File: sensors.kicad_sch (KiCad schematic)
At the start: 16 parts, among them Q1 TEFT4300, Q2 TEFT4300, Q5 Q_NMOS_DGS

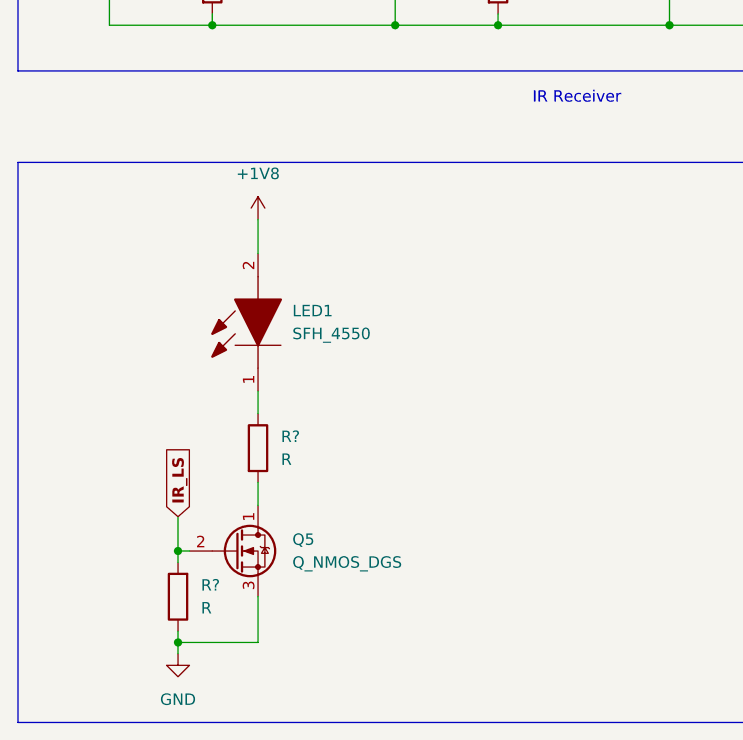
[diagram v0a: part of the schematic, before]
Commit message: begin IR Tx
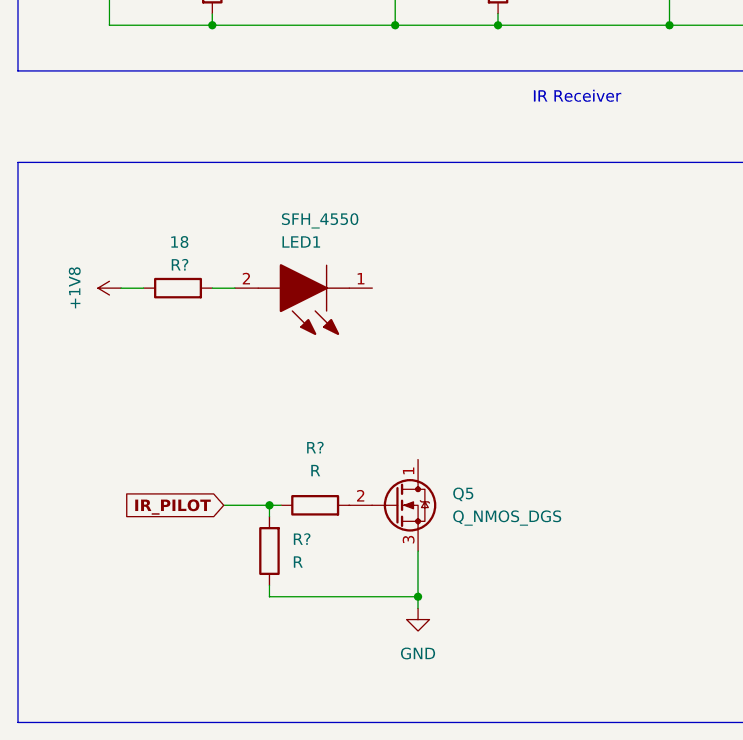
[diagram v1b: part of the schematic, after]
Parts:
- added R?: R, symbol Device:R
- R?: value R -> 18
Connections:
- net +1V8: now also R?.1; no longer LED1.2
- net at LED1.1: no longer R?.1
- net at R?.2: now also LED1.2; no longer Q5.1 (D)
- net IR_LS: no longer names the net of Q5.2 (G)
- net IR_LS: now also R?.2; no longer R?.2
- new net IR_PILOT: R?.1, R?.2
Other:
- moved on the sheet: LED1, Q5, R?

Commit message: Update sensors.kicad_sch
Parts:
- removed LED1: SFH_4550, SFH4550, symbol SFH_4550:SFH_4550
- removed R?: 18, symbol Device:R
- added LED? (x2): SFH_4550, SFH4550, symbol SFH_4550:SFH_4550
- added Q?: Q_NMOS_DGS, symbol Device:Q_NMOS_DGS
- added R? (x4): R, symbol Device:R
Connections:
- net +1V8: now also LED?.2, LED?.2
- net GND: now also Q?.3 (S), R?.1
- net IR_PILOT: now also R?.1, R?.2
- net at Q5.1 (D): now also R?.2
- new net: LED?.1, R?.1 (x2)
- new net: Q?.1 (D), R?.2
- new net: Q?.2 (G), R?.2

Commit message: finish IR transmitters
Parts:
- removed LED?: SFH_4550, SFH4550, symbol SFH_4550:SFH_4550
- removed Q5: Q_NMOS_DGS, symbol Device:Q_NMOS_DGS
- removed R? (x4): R, symbol Device:R
- added C? (x5): 0.1u, symbol Device:C
- added C? (x5): 4,7u, symbol Device:C
- added LED? (x4): SFH_4550, SFH4550, symbol SFH_4550:SFH_4550
- added Q? (x4): Q_NMOS_DGS, symbol Device:Q_NMOS_DGS
- added R? (x4): 10k, symbol Device:R
- added R? (x4): 0.56, symbol Device:R
- R?: value R -> 10k
- R?: value R -> 0.56
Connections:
- net +1V8: now also C?.1, C?.1, C?.1, C?.1, C?.1, C?.1, C?.1, C?.1, C?.1, C?.1, LED?.2, LED?.2, LED?.2, LED?.2
- net GND: now also C?.2, C?.2, C?.2, C?.2, C?.2, C?.2, C?.2, C?.2, C?.2, C?.2, Q?.3 (S), Q?.3 (S), Q?.3 (S), Q?.3 (S), R?.1, R?.1, R?.1, R?.1
- net IR_PILOT: now also Q?.2 (G), Q?.2 (G), Q?.2 (G), Q?.2 (G), Q?.2 (G), R?.2, R?.2, R?.2, R?.2
- new net: LED?.1, R?.1 (x4)
- new net: Q?.1 (D), R?.2 (x4)
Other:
- note added: "IR Transmitters"
- moved on the sheet: LED?, Q?, R?
